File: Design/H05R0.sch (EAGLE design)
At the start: 59 parts, among them Q1 ECH8693R-TL-W, U1 STM32G0B1CEU6N, U2 MAX17330X22+, U3 TPS631000DRLR, U4 LD39200PU33R, X1 XTALL_CSTCE8M00G52

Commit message: -Standarize the files and folders
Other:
- note added: "H05R0"
- note added: "H05R0_Backend"
- note added: "H05R0_Frontend"
- note removed: "H05R00"
- note removed: "H05R00_Backend"
- note removed: "H05R00_Frontend"
- note removed: "Ibrahim Zaeiter"
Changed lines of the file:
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@@
 <text x="216.45" y="4.9548" size="1.9304" layer="100" font="vector">Sheet   of</text>
 <text x="200.0162" y="19.2042" size="1.9304" layer="100" font="vector">Title</text>
-<text x="181.4742" y="19.2042" size="1.9304" layer="102" font="vector">H05R00</text>
+<text x="181.4742" y="19.2042" size="1.9304" layer="102" font="vector">H05R0</text>
 <text x="170.2728" y="10.7714" size="1.9304" layer="101" font="vector">1s Lipo charger w/ USB-C </text>
-<text x="206.8742" y="19.2042" size="1.9304" layer="101" font="vector">H05R00_Backend</text>
+<text x="206.8742" y="19.2042" size="1.9304" layer="101" font="vector">H05R0_Backend</text>
 <wire x1="169.46" y1="3.38" x2="169.46" y2="7.698" width="0.1524" layer="205"/>
 <wire x1="169.46" y1="7.698" x2="169.46" y2="17.858" width="0.1524" layer="205"/>
@@
 <wire x1="231.69" y1="17.858" x2="231.69" y2="22.43" width="0.1524" layer="205"/>
 <text x="243.1962" y="5.7422" size="1.9304" layer="100" font="vector">www.hexabitz.com</text>
-<text x="182.7442" y="4.5992" size="1.9304" layer="101" font="vector">Ibrahim Zaeiter</text>
 <text x="254.635" y="142.24" size="1.778" layer="95">BOOT</text>
 </plain>
@@
 <text x="216.45" y="4.9548" size="1.9304" layer="100" font="vector">Sheet   of</text>
 <text x="200.0162" y="19.2042" size="1.9304" layer="100" font="vector">Title</text>
-<text x="181.4742" y="19.2042" size="1.9304" layer="102" font="vector">H05R00</text>
+<text x="181.4742" y="19.2042" size="1.9304" layer="102" font="vector">H05R0</text>
 <text x="170.2728" y="10.7714" size="1.9304" layer="101" font="vector">1s Lipo charger w/ USB-C </text>
-<text x="206.8742" y="19.2042" size="1.9304" layer="101" font="vector">H05R00_Frontend</text>
+<text x="206.8742" y="19.2042" size="1.9304" layer="101" font="vector">H05R0_Frontend</text>
 <wire x1="169.46" y1="3.38" x2="169.46" y2="7.698" width="0.1524" layer="205"/>
 <wire x1="169.46" y1="7.698" x2="169.46" y2="17.858" width="0.1524" layer="205"/>
@@
 <wire x1="231.69" y1="17.858" x2="231.69" y2="22.43" width="0.1524" layer="205"/>
 <text x="243.1962" y="5.7422" size="1.9304" layer="100" font="vector">www.hexabitz.com</text>
-<text x="184.0142" y="4.5992" size="1.9304" layer="101" font="vector">Ibrahim Zaeiter</text>
+<text x="184.0142" y="4.5992" size="1.9304" layer="101" font="vector"></text>
 <text x="100.33" y="135.89" size="3.81" layer="101">Buck-Boost Converter</text>
 <text x="212.725" y="135.255" size="3.81" layer="101">LDO Regulator</text>

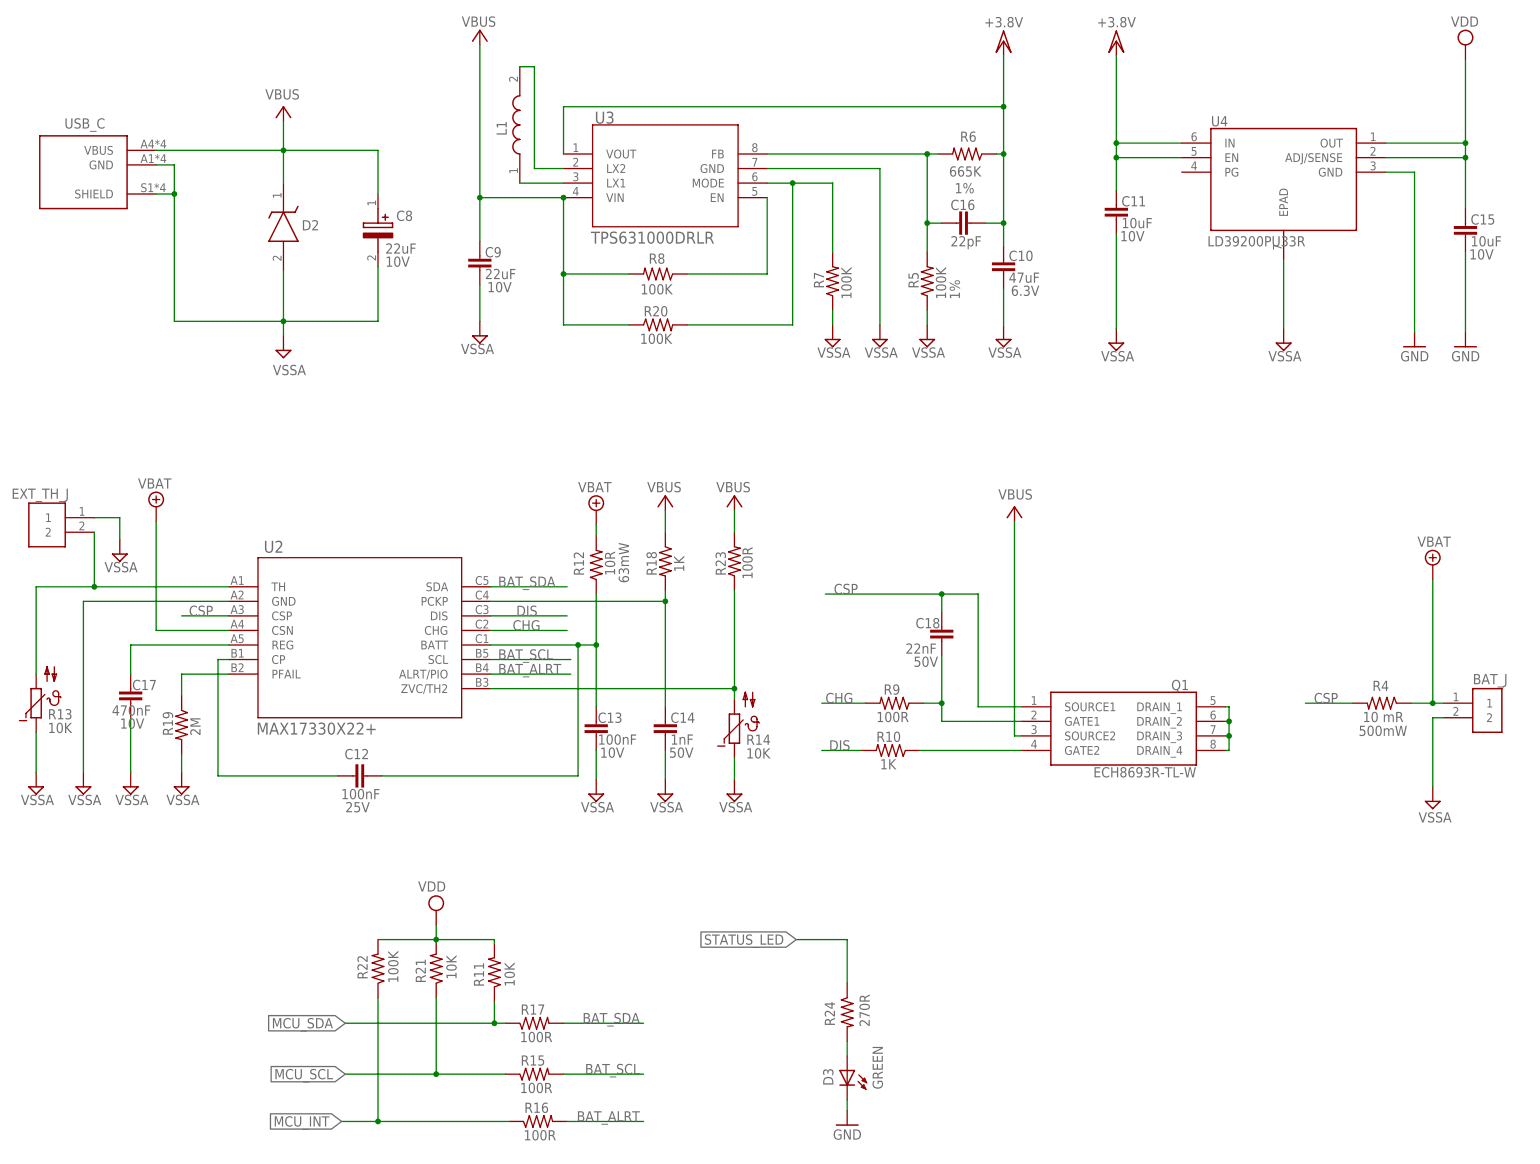
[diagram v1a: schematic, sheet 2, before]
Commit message: -Adding wire to board terminal block
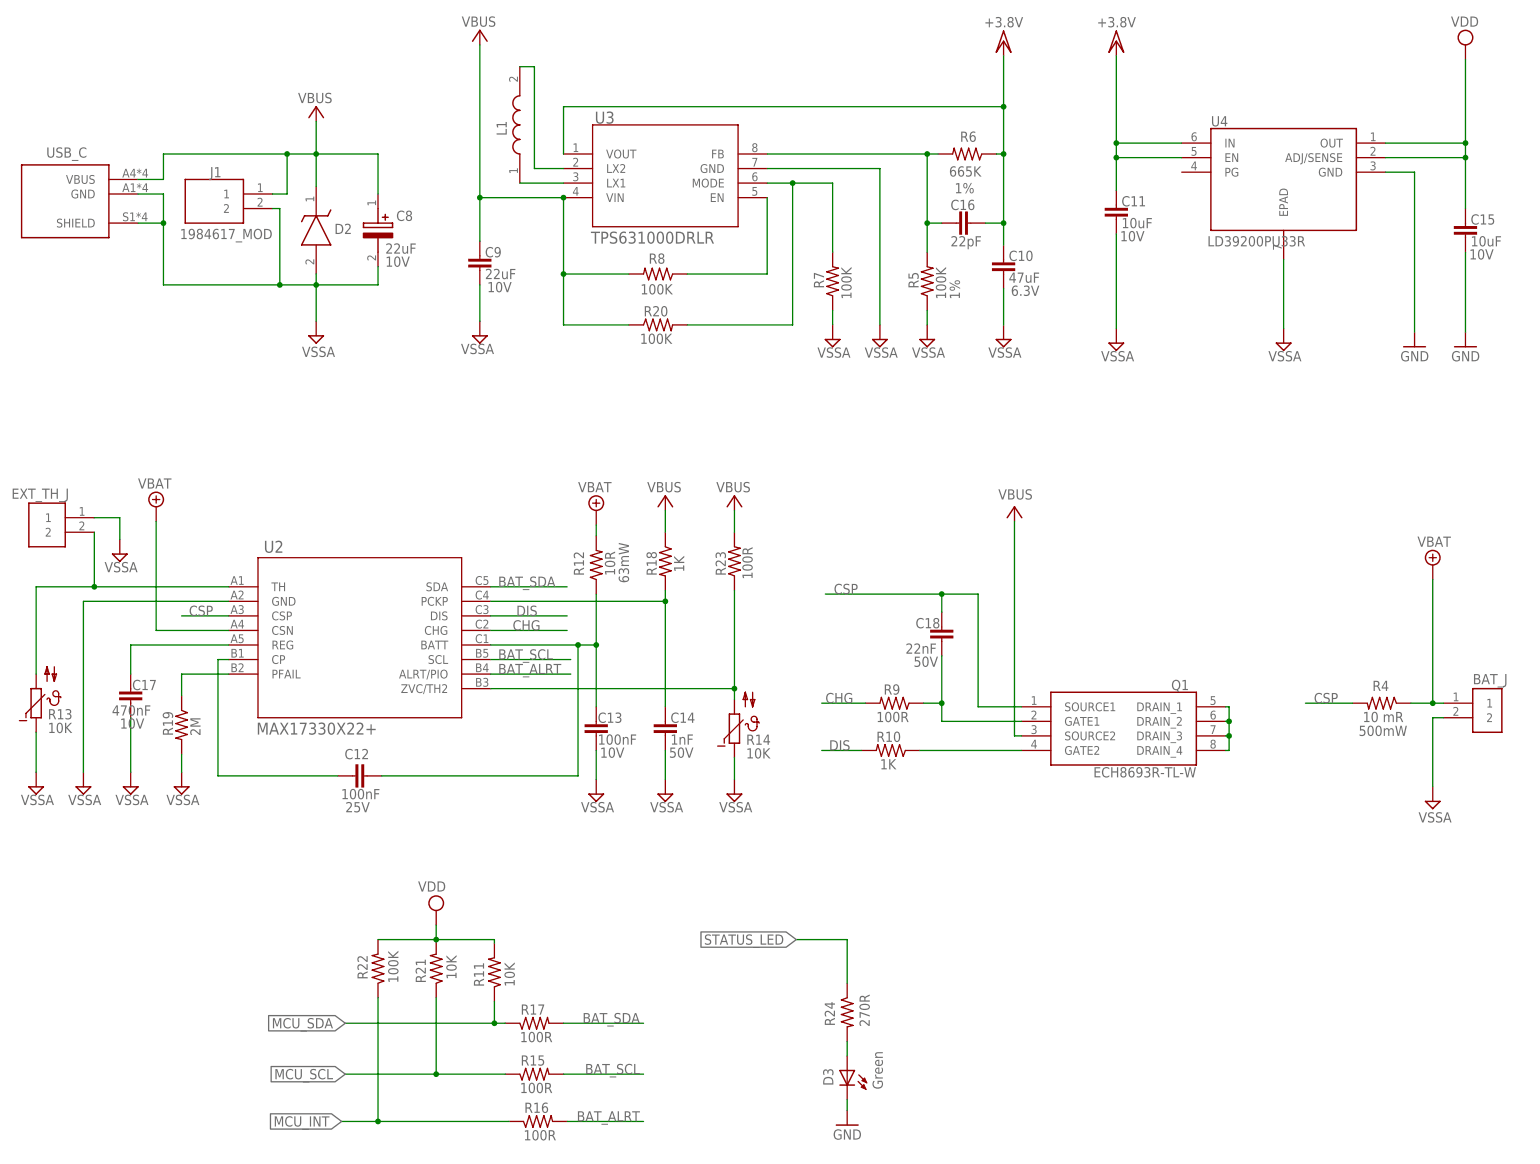
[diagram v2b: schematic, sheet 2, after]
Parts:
- added J1: 1984617_MOD, HEXABITZ_CONNECTION_PARTS:1984617_MOD
- D1: device Hexabitz:VLMS1300-GS08 -> HEXABITZ_USER_INTERFACE_PARTS:VLMS1300-GS08
- D3: value GREEN -> Green; device Hexabitz:VLMS1300-GS08 -> HEXABITZ_USER_INTERFACE_PARTS:VLMTG1300-GS08
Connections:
- net VBUS: now also J1.1
- net VSSA: now also J1.2
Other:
- moved on the sheet: D2, USB_C
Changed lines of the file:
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@@
 <?xml version="1.0" encoding="utf-8"?>
 <!DOCTYPE eagle SYSTEM "eagle.dtd">
-<eagle version="9.6.2">
+<eagle version="9.6.1">
 <drawing>
 <settings>
@@
 <setting verticaltext="up"/>
 </settings>
-<grid distance="25" unitdist="mil" unit="mil" style="lines" multiple="1" display="yes" altdistance="0.01" altunitdist="inch" altunit="inch"/>
+<grid distance="0.1" unitdist="inch" unit="inch" style="lines" multiple="1" display="no" altdistance="0.01" altunitdist="inch" altunit="inch"/>
 <layers>
 <layer number="1" name="Top" color="4" fill="1" visible="no" active="no"/>
@@
 </classes>
 <parts>
-<part name="D1" library="Hexabitz" deviceset="VLMS1300-GS08" device="" package3d_urn="urn:adsk.eagle:package:20064571/2" value="RED">
+<part name="D1" library="HEXABITZ_USER_INTERFACE_PARTS" library_urn="urn:adsk.eagle:library:20064563" deviceset="VLMS1300-GS08" device="" package3d_urn="urn:adsk.eagle:package:20064571/3" value="RED">
 <attribute name="MFN" value="Vishay"/>
 <attribute name="MPN" value="VLMS1300-GS08"/>
@@
 <attribute name="STATE" value="DNP"/>
 </part>
-<part name="EXT_TH_J" library="HEXABITZ_USER_INTERFACE_PARTS" library_urn="urn:adsk.eagle:library:20064563" deviceset="3-644456-2" device="" package3d_urn="urn:adsk.eagle:package:20064570/4"/>
+<part name="EXT_TH_J" library="HEXABITZ_USER_INTERFACE_PARTS" library_urn="urn:adsk.eagle:library:20064563" deviceset="3-644456-2" device="" package3d_urn="urn:adsk.eagle:package:20064570/5"/>
 <part name="SUPPLY39" library="HEXABITZ_CONNECTION_PARTS" library_urn="urn:adsk.eagle:library:20064553" deviceset="VSSA" device=""/>
 <part name="R11" library="HEXABITZ_RCLS" library_urn="urn:adsk.eagle:library:20064561" deviceset="R-0603" device="" package3d_urn="urn:adsk.eagle:package:1435818/6" value="10K"/>
@@
 <part name="R22" library="HEXABITZ_RCLS" library_urn="urn:adsk.eagle:library:20064561" deviceset="R-0603" device="" package3d_urn="urn:adsk.eagle:package:1435818/6" value="100K"/>
 <part name="SUPPLY28" library="supply2" library_urn="urn:adsk.eagle:library:372" deviceset="VDD" device=""/>
-<part name="D3" library="Hexabitz" deviceset="VLMS1300-GS08" device="" package3d_urn="urn:adsk.eagle:package:20064571/2" value="GREEN">
+<part name="D3" library="HEXABITZ_USER_INTERFACE_PARTS" library_urn="urn:adsk.eagle:library:20064563" deviceset="VLMTG1300-GS08" device="" package3d_urn="urn:adsk.eagle:package:27845960/3" value="Green">
 <attribute name="MFN" value="Vishay"/>
 <attribute name="MPN" value="VLMS1300-GS08"/>
@@
 <part name="GND13" library="supply1" deviceset="GND" device=""/>
 <part name="R24" library="HEXABITZ_RCLS" library_urn="urn:adsk.eagle:library:20064561" deviceset="R-0603" device="" package3d_urn="urn:adsk.eagle:package:1435818/6" value="270R"/>
+<part name="J1" library="HEXABITZ_CONNECTION_PARTS" library_urn="urn:adsk.eagle:library:20064553" deviceset="1984617_MOD" device="" package3d_urn="urn:adsk.eagle:package:43389157/1"/>
 </parts>
 <sheets>
@@
 <attribute name="NAME" x="263.520640625" y="87.76266875" size="1.78105" layer="95"/>
 </instance>
-<instance part="D2" gate="G$1" x="55.88" y="175.26" smashed="yes" rot="R270">
-<attribute name="NAME" x="59.055" y="167.005" size="1.778" layer="95"/>
+<instance part="D2" gate="G$1" x="61.595" y="174.625" smashed="yes" rot="R270">
+<attribute name="NAME" x="64.77" y="166.37" size="1.778" layer="95"/>
 </instance>
 <instance part="C8" gate="G$1" x="72.39" y="173.355" smashed="yes" rot="R270">
@@
 <attribute name="VOLTAGE" x="73.66" y="160.655" size="1.778" layer="96"/>
 </instance>
-<instance part="SUPPLY2" gate="G$1" x="55.88" y="146.05" smashed="yes">
-<attribute name="VALUE" x="59.817" y="143.51" size="1.778" layer="96" rot="R180"/>
+<instance part="SUPPLY2" gate="G$1" x="61.595" y="148.59" smashed="yes">
+<attribute name="VALUE" x="64.897" y="146.685" size="1.778" layer="96" rot="R180"/>
 </instance>
 <instance part="SUPPLY5" gate="G$1" x="256.54" y="67.31" smashed="yes">
@@
 <attribute name="VOLTAGE_RATING" x="262.89" y="161.925" size="1.778" layer="96"/>
 </instance>
-<instance part="SUPPLY32" gate="G$1" x="55.88" y="188.595" smashed="yes">
-<attribute name="VALUE" x="52.705" y="189.865" size="1.778" layer="96"/>
+<instance part="SUPPLY32" gate="G$1" x="61.595" y="188.595" smashed="yes">
+<attribute name="VALUE" x="58.42" y="189.23" size="1.778" layer="96"/>
 </instance>
 <instance part="SUPPLY34" gate="G$1" x="183.515" y="118.745" smashed="yes" rot="MR0">
@@
 <attribute name="VALUE" x="198.628" y="144.145" size="1.778" layer="96"/>
 </instance>
-<instance part="USB_C" gate="G$1" x="20.955" y="178.435" smashed="yes" rot="MR0">
-<attribute name="NAME" x="24.765" y="184.785" size="1.778" layer="95" rot="MR0"/>
+<instance part="USB_C" gate="G$1" x="17.78" y="173.355" smashed="yes" rot="MR0">
+<attribute name="NAME" x="21.59" y="179.705" size="1.778" layer="95" rot="MR0"/>
 </instance>
 <instance part="SUPPLY38" gate="G$1" x="110.49" y="118.11" smashed="yes">
@@
 <attribute name="VALUE" x="158.242" y="33.655" size="1.778" layer="96" rot="MR270"/>
 </instance>
+<instance part="J1" gate="G$1" x="53.975" y="173.355" smashed="yes" rot="MR0">
+<attribute name="NAME" x="45.085" y="177.165" size="1.778" layer="95" rot="MR0" align="center-left"/>
+<attribute name="VALUE" x="53.975" y="166.37" size="1.778" layer="96" rot="MR0" align="center-left"/>
+</instance>
 </instances>
 <busses>
@@
 <segment>
 <pinref part="SUPPLY2" gate="G$1" pin="AGND"/>
-<wire x1="55.88" y1="148.59" x2="55.88" y2="151.13" width="0.1524" layer="91"/>
-<wire x1="36.83" y1="173.355" x2="36.83" y2="151.13" width="0.1524" layer="91"/>
-<wire x1="72.39" y1="151.13" x2="55.88" y2="151.13" width="0.1524" layer="91"/>
-<wire x1="55.88" y1="151.13" x2="36.83" y2="151.13" width="0.1524" layer="91"/>
+<wire x1="61.595" y1="151.13" x2="61.595" y2="157.48" width="0.1524" layer="91"/>
+<wire x1="72.39" y1="157.48" x2="61.595" y2="157.48" width="0.1524" layer="91"/>
+<wire x1="61.595" y1="157.48" x2="55.245" y2="157.48" width="0.1524" layer="91"/>
 <pinref part="C8" gate="G$1" pin="-"/>
-<wire x1="72.39" y1="160.655" x2="72.39" y2="151.13" width="0.1524" layer="91"/>
+<wire x1="55.245" y1="157.48" x2="34.925" y2="157.48" width="0.1524" layer="91"/>
+<wire x1="72.39" y1="160.655" x2="72.39" y2="157.48" width="0.1524" layer="91"/>
 <pinref part="D2" gate="G$1" pin="A"/>
-<wire x1="55.88" y1="160.02" x2="55.88" y2="151.13" width="0.1524" layer="91"/>
-<junction x="55.88" y="151.13"/>
-<pinref part="USB_C" gate="G$1" pin="SHIELD"/>
-<wire x1="36.83" y1="173.355" x2="33.655" y2="173.355" width="0.1524" layer="91"/>
+<wire x1="61.595" y1="159.385" x2="61.595" y2="157.48" width="0.1524" layer="91"/>
+<junction x="61.595" y="157.48"/>
 <pinref part="USB_C" gate="G$1" pin="GND"/>
-<wire x1="33.655" y1="178.435" x2="36.83" y2="178.435" width="0.1524" layer="91"/>
-<wire x1="36.83" y1="178.435" x2="36.83" y2="173.355" width="0.1524" layer="91"/>
-<junction x="36.83" y="173.355"/>
+<wire x1="30.48" y1="173.355" x2="34.925" y2="173.355" width="0.1524" layer="91"/>
+<wire x1="34.925" y1="173.355" x2="34.925" y2="168.275" width="0.1524" layer="91"/>
+<pinref part="USB_C" gate="G$1" pin="SHIELD"/>
+<wire x1="34.925" y1="168.275" x2="34.925" y2="157.48" width="0.1524" layer="91"/>
+<wire x1="30.48" y1="168.275" x2="34.925" y2="168.275" width="0.1524" layer="91"/>
+<junction x="34.925" y="168.275"/>
+<pinref part="J1" gate="G$1" pin="2"/>
+<wire x1="53.975" y1="170.815" x2="55.245" y2="170.815" width="0.1524" layer="91"/>
+<wire x1="55.245" y1="170.815" x2="55.245" y2="157.48" width="0.1524" layer="91"/>
+<junction x="55.245" y="157.48"/>
 </segment>
 <segment>
@@
 <net name="VBUS" class="0">
 <segment>
-<wire x1="33.655" y1="180.975" x2="55.88" y2="180.975" width="0.1524" layer="91"/>
 <pinref part="D2" gate="G$1" pin="K"/>
-<wire x1="55.88" y1="180.975" x2="72.39" y2="180.975" width="0.1524" layer="91"/>
-<wire x1="55.88" y1="175.26" x2="55.88" y2="180.975" width="0.1524" layer="91"/>
-<junction x="55.88" y="180.975"/>
+<wire x1="61.595" y1="180.34" x2="72.39" y2="180.34" width="0.1524" layer="91"/>
+<wire x1="61.595" y1="174.625" x2="61.595" y2="180.34" width="0.1524" layer="91"/>
+<junction x="61.595" y="180.34"/>
 <pinref part="C8" gate="G$1" pin="+"/>
-<wire x1="72.39" y1="173.355" x2="72.39" y2="180.975" width="0.1524" layer="91"/>
-<wire x1="55.88" y1="186.055" x2="55.88" y2="180.975" width="0.1524" layer="91"/>
+<wire x1="72.39" y1="173.355" x2="72.39" y2="180.34" width="0.1524" layer="91"/>
+<wire x1="61.595" y1="186.055" x2="61.595" y2="180.34" width="0.1524" layer="91"/>
 <pinref part="SUPPLY32" gate="G$1" pin="VBUS"/>
+<pinref part="J1" gate="G$1" pin="1"/>
+<wire x1="61.595" y1="180.34" x2="56.515" y2="180.34" width="0.1524" layer="91"/>
 <pinref part="USB_C" gate="G$1" pin="VBUS"/>
+<wire x1="56.515" y1="180.34" x2="56.515" y2="173.355" width="0.1524" layer="91"/>
+<wire x1="56.515" y1="173.355" x2="53.975" y2="173.355" width="0.1524" layer="91"/>
+<wire x1="30.48" y1="175.895" x2="34.925" y2="175.895" width="0.1524" layer="91"/>
+<wire x1="34.925" y1="175.895" x2="34.925" y2="180.34" width="0.1524" layer="91"/>
+<wire x1="34.925" y1="180.34" x2="56.515" y2="180.34" width="0.1524" layer="91"/>
+<junction x="56.515" y="180.34"/>
 </segment>
 <segment>

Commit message: -Update the logo and add TVS
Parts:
- added D4: BOURNS_CDSOD323-T03SCBOURNS_CDSOD323-T03SC_0_0, HEXABITZ_RCLS:BOURNS_CDSOD323-T03SCBOURNS_CDSOD323-T03SC_0_0
- added TRIMBLE-LOGO1: HEXA-LOGO, HEXABITZ_USER_INTERFACE_PARTS:HEXA-LOGO
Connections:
- net GND: now also D4.A
- net VDD: now also D4.C

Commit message: Unreviewed version - update the design by adding additional transistors in parallel.
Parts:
- removed C6: 100nF, HEXABITZ_RCLS:C-0603
- removed C7: 4.7uF, HEXABITZ_RCLS:C-0805-POL
- added Q2: ECH8693R-TL-W, HEXABITZ_RCLS:ECH8693R-TL-W
- added U5: NCP45521IMNTWG-LDFN8_2X2_ONS, HEXABITZ_ICs:NCP45521IMNTWG-LDFN8_2X2_ONS
- U1: value STM32G0B1CEU6N -> STM32G0B1CEU6QFN_B1CEU6_STM-L; device HEXABITZ_ICs:STM32G0B1CEU6N -> HEXABITZ_ICs:STM32G0B1CEU6QFN_B1CEU6_STM-L
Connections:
- new net N$4: Q2.DRAIN_1, Q2.DRAIN_2, Q2.DRAIN_3, Q2.DRAIN_4
- net CSP: now also Q2.SOURCE1
- net GND: no longer C6.2, C7.-, U1.EPAD
- net N$10: now also Q2.GATE1
- net N$15: now also Q2.GATE2
- net VBUS: now also Q2.SOURCE2
- net VDD: no longer C6.1, C7.+, U1.VDDIO2
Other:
- note added: "Charge & Discharge N-FETs"
- note removed: "0"
- note removed: "Charge & Discharge N-FET"
- note removed: "VDDIO2 Coupling"
- moved on the sheet: BAT_J, D4, R4
